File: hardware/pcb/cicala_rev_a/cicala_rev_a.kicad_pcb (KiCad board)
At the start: 4 copper layers, 78 x 45 mm, 0 parts

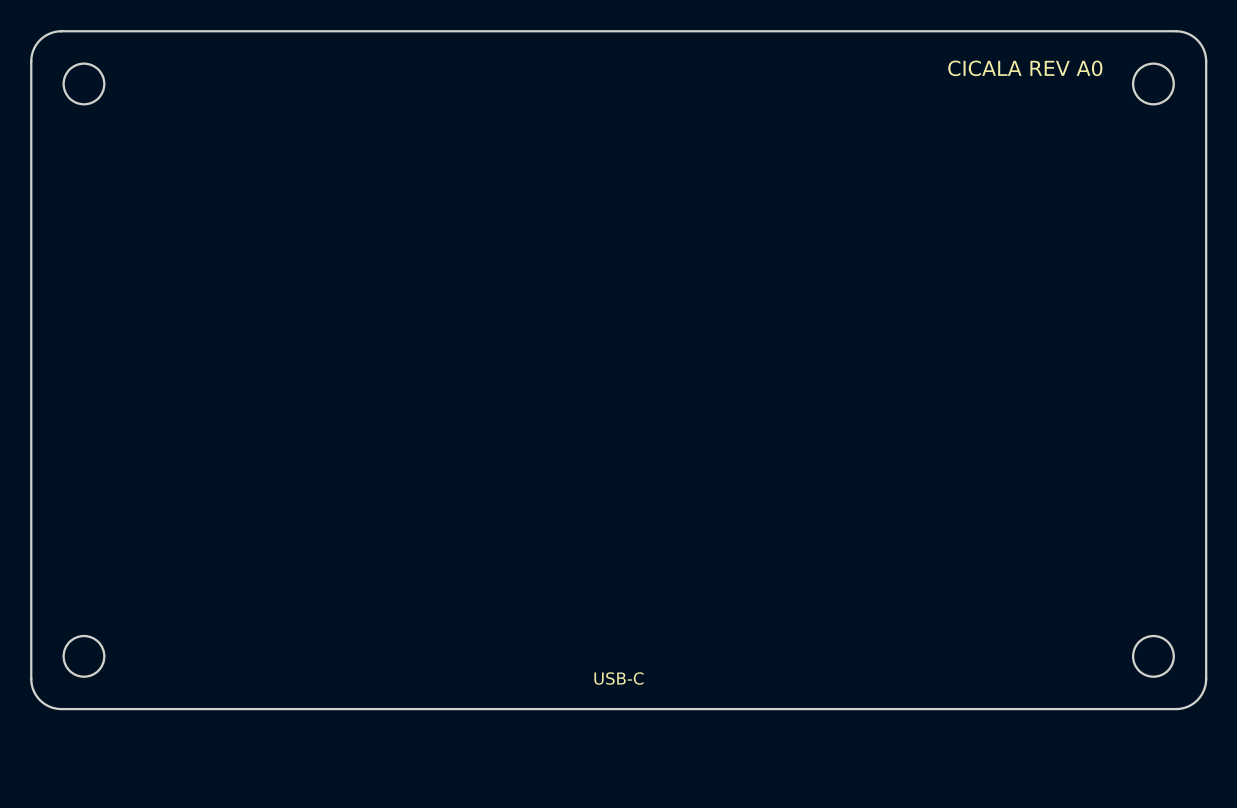
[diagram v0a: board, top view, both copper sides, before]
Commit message: feat(hw): place the Rev A board
Everything except the two switches and the display stack sits on the
underside, in the cell cavity, because the sloped roof leaves 0.8 to 3.5 mm
above the board. The module goes rear-left with its antenna at the board
edge and clear of the display; the cell keep-out, the power block and the
front connector row follow from that.

Placement is generated rather than dragged, so it can be regenerated after a
schematic change: anchors are chosen by hand, the rest are packed into free
regions ordered by distance to the pads they already share a net with.

Board is 78 x 49 mm at (3, 3.5). It grew 4 mm deeper than the old 78 x 45
because a USB-C plug could never have reached a receptacle sitting 6 mm
behind the case wall; the front edge now ends 1.5 mm from it and the
receptacle noses into the wall aperture.

Mounting holes become NPTH footprints instead of circles on Edge.Cuts, so
they are drilled rather than routed, and they move to x=13 to clear
Espressif's antenna keep-out, which the module footprint carries and which
reaches 9.5 mm in from the left edge.

J1 gets a project footprint whose silkscreen stops at the board edge; the
library outline would print past it, because the part deliberately overhangs.

Netclasses: Power 0.4 mm, USB 0.29 mm at a 0.29 mm gap for 90 ohm
differential over the declared 0.18 mm prepreg, HV 0.2 mm, which is the gap
the panel's own 0.5 mm-pitch connector allows.

DRC reports zero violations and zero schematic-parity issues. The 216
unconnected items are the routing, which is the next commit.

Co-Authored-By: Claude Opus 5 <noreply@anthropic.com>
Claude-Session: https://claude.ai/code/session_01E5vy1HJsPztSk9nFw6j5Ko
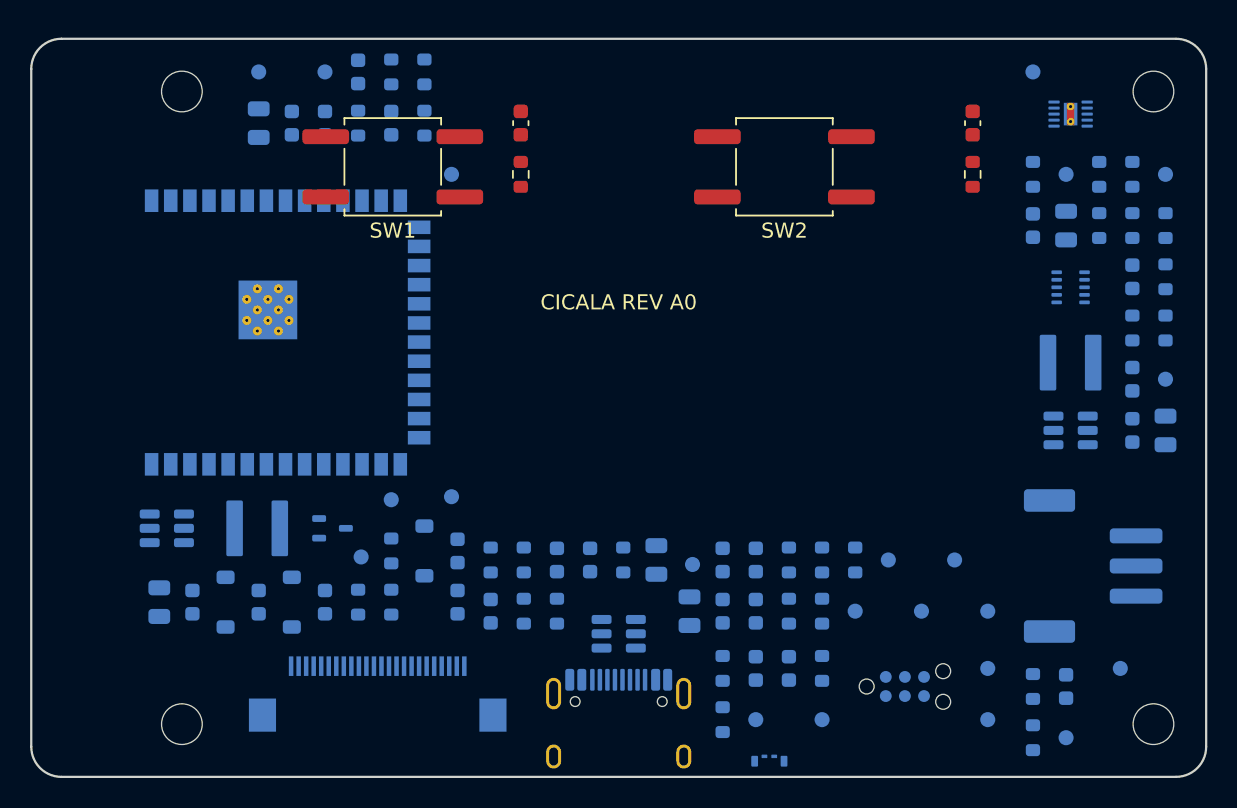
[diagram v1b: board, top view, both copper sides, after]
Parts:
- added C1: 3pF DNP, Capacitor_SMD:C_0603_1608Metric, B.Cu at (37.9, 38.1)
- added C10: 47uF 6.3V, Capacitor_SMD:C_0805_2012Metric, B.Cu at (78.3, 29.5)
- added C11: 100nF, Capacitor_SMD:C_0603_1608Metric, B.Cu at (76.1, 26.1)
- added C12: 1uF, Capacitor_SMD:C_0603_1608Metric, B.Cu at (22.5, 40.9)
- added C13: 10uF, Capacitor_SMD:C_0603_1608Metric, B.Cu at (18.1, 40.9)
- added C14: 1nF, Capacitor_SMD:C_0603_1608Metric, B.Cu at (13.7, 40.9)
- added C15: 4.7uF 25V, Capacitor_SMD:C_0805_2012Metric, B.Cu at (11.5, 40.9)
- added C16: 4.7uF 25V, Capacitor_SMD:C_0805_2012Metric, B.Cu at (44.5, 38.1)
- added C17: 1uF 25V, Capacitor_SMD:C_0603_1608Metric, B.Cu at (31.3, 40.9)
- added C18: 1uF 25V, Capacitor_SMD:C_0603_1608Metric, B.Cu at (33.5, 41.5)
- added C19: 1uF 25V, Capacitor_SMD:C_0603_1608Metric, B.Cu at (31.3, 37.5)
- added C2: 3pF DNP, Capacitor_SMD:C_0603_1608Metric, B.Cu at (40.1, 38.1)
- added C20: 1uF 25V, Capacitor_SMD:C_0603_1608Metric, B.Cu at (48.9, 41.5)
- added C21: 1uF 25V, Capacitor_SMD:C_0603_1608Metric, B.Cu at (51.1, 45.3)
- added C22: 1uF 25V, Capacitor_SMD:C_0603_1608Metric, B.Cu at (51.1, 41.5)
- added C23: 1uF 25V, Capacitor_SMD:C_0603_1608Metric, B.Cu at (51.1, 38.1)
- added C24: 1uF 25V, Capacitor_SMD:C_0603_1608Metric, B.Cu at (53.3, 45.3)
- added C25: 10nF, Capacitor_SMD:C_0603_1608Metric, F.Cu at (35.5, 9.10)
- added C26: 10nF, Capacitor_SMD:C_0603_1608Metric, F.Cu at (65.5, 9.10)
- added C27: 1uF, Capacitor_SMD:C_0603_1608Metric, B.Cu at (26.9, 9.10)
- added C28: 100nF, Capacitor_SMD:C_0603_1608Metric, B.Cu at (20.3, 9.10)
- added C29: 10uF, Capacitor_SMD:C_0603_1608Metric, B.Cu at (22.5, 9.10)
- added C3: 100nF, Capacitor_SMD:C_0603_1608Metric, B.Cu at (24.7, 5.70)
- added C30: 47uF, Capacitor_SMD:C_0805_2012Metric, B.Cu at (18.1, 9.10)
- added C31: 1nF 2kV, Capacitor_SMD:C_0805_2012Metric, B.Cu at (46.7, 41.5)
- added C4: 1uF 25V, Capacitor_SMD:C_0603_1608Metric, B.Cu at (48.9, 38.1)
- added C5: 10uF 25V, Capacitor_SMD:C_0805_2012Metric, B.Cu at (71.7, 15.9)
- added C6: 1uF 10V, Capacitor_SMD:C_0603_1608Metric, B.Cu at (69.5, 15.9)
- added C7: 100nF, Capacitor_SMD:C_0603_1608Metric, B.Cu at (71.7, 46.5)
- added C8: 10uF 6.3V, Capacitor_SMD:C_0603_1608Metric, B.Cu at (76.1, 19.3)
- added C9: 22uF 6.3V, Capacitor_SMD:C_0603_1608Metric, B.Cu at (76.1, 29.5)
- added D1: MBR0530, Diode_SMD:D_SOD-123, B.Cu at (20.3, 40.9)
- added D2: MBR0530, Diode_SMD:D_SOD-123, B.Cu at (15.9, 40.9)
- added D3: MBR0530, Diode_SMD:D_SOD-123, B.Cu at (29.1, 37.5)
- added D4: APBA2006SURKCGKC red/green, cicala:LED_Kingbright_APBA2006SURKCGKC, B.Cu at (52.0, 51.3)
- added H1: M2.5, MountingHole_2.7mm, F.Cu at (13.0, 7.00)
- added H2: M2.5, MountingHole_2.7mm, F.Cu at (77.5, 7.00)
- added H3: M2.5, MountingHole_2.7mm, F.Cu at (13.0, 49.0)
- added H4: M2.5, MountingHole_2.7mm, F.Cu at (77.5, 49.0)
- added J1: USB-C receptacle, cicala:USB_C_Receptacle_HRO_TYPE-C-31-M-12_EdgeOverhang, B.Cu at (42.0, 50.1)
- added J2: GDEY0213B74, Connector_FFC-FPC:Hirose_FH12-24S-0.5SH_1x24-1MP_P0.50mm_Horizontal, B.Cu at (26.0, 47.0)
- added J3: Protected LiPo + NTC, Connector_JST:JST_PH_S3B-PH-SM4-TB_1x03-1MP_P2.00mm_Horizontal, B.Cu at (73.5, 38.5)
- added J4: TC2030 recovery pads, Connector:Tag-Connect_TC2030-IDC-NL_2x03_P1.27mm_Vertical, B.Cu at (61.0, 46.5)
- added L1: 47uH VLS4012CX-470M-1, cicala:L_TDK_VLS4012, B.Cu at (18.0, 36.0)
- added L2: 0.47uH XFL4015-471ME, cicala:L_Coilcraft_XFL4015, B.Cu at (72.0, 25.0)
- added Q1: Si1308EDL, Package_TO_SOT_SMD:SOT-323_SC-70, B.Cu at (23.0, 36.0)
- added R1: 5.1k, Resistor_SMD:R_0603_1608Metric, B.Cu at (48.9, 45.3)
- added R10: 10k, Resistor_SMD:R_0603_1608Metric, B.Cu at (73.9, 15.9)
- added R11: 1M, Resistor_SMD:R_0603_1608Metric, B.Cu at (69.5, 46.5)
- added R12: 470k, Resistor_SMD:R_0603_1608Metric, B.Cu at (69.5, 49.9)
- added R13: 100k, Resistor_SMD:R_0603_1608Metric, B.Cu at (76.1, 15.9)
- added R14: 511k 1%, Resistor_SMD:R_0603_1608Metric, B.Cu at (76.1, 22.7)
- added R15: 91k 1%, Resistor_SMD:R_0603_1608Metric, B.Cu at (78.3, 19.3)
- added R16: 100k, Resistor_SMD:R_0603_1608Metric, B.Cu at (78.3, 15.9)
- added R18: 150, Resistor_SMD:R_0603_1608Metric, B.Cu at (26.9, 37.5)
- added R19: 1M, Resistor_SMD:R_0603_1608Metric, B.Cu at (26.9, 40.9)
- added R2: 5.1k, Resistor_SMD:R_0603_1608Metric, B.Cu at (37.9, 41.5)
- added R20: 2.2, Resistor_SMD:R_0603_1608Metric, B.Cu at (24.7, 40.9)
- added R21: 47k, Resistor_SMD:R_0603_1608Metric, F.Cu at (35.5, 12.5)
- added R22: 47k, Resistor_SMD:R_0603_1608Metric, F.Cu at (65.5, 12.5)
- added R23: 1k, Resistor_SMD:R_0603_1608Metric, B.Cu at (42.3, 38.1)
- added R24: 1k, Resistor_SMD:R_0603_1608Metric, B.Cu at (35.7, 41.5)
- added R25: 10k, Resistor_SMD:R_0603_1608Metric, B.Cu at (29.1, 9.10)
- added R26: 10k, Resistor_SMD:R_0603_1608Metric, B.Cu at (24.7, 9.10)
- added R27: 470, Resistor_SMD:R_0603_1608Metric, B.Cu at (53.3, 38.1)
- added R28: 470, Resistor_SMD:R_0603_1608Metric, B.Cu at (53.3, 41.5)
- added R29: 470, Resistor_SMD:R_0603_1608Metric, B.Cu at (55.5, 38.1)
- added R3: 22, Resistor_SMD:R_0603_1608Metric, B.Cu at (35.7, 38.1)
- added R30: 470, Resistor_SMD:R_0603_1608Metric, B.Cu at (55.5, 41.5)
- added R31: 470, Resistor_SMD:R_0603_1608Metric, B.Cu at (57.7, 38.1)
- added R32: 1M, Resistor_SMD:R_0603_1608Metric, B.Cu at (55.5, 45.3)
- added R33: 0, Resistor_SMD:R_0603_1608Metric, B.Cu at (48.9, 48.7)
- added R34: 0, Resistor_SMD:R_0603_1608Metric, B.Cu at (78.3, 22.7)
- added R4: 22, Resistor_SMD:R_0603_1608Metric, B.Cu at (33.5, 38.1)
- added R5: 100k, Resistor_SMD:R_0603_1608Metric, B.Cu at (29.1, 5.70)
- added R6: 150k, Resistor_SMD:R_0603_1608Metric, B.Cu at (26.9, 5.70)
- added R7: 18k, Resistor_SMD:R_0603_1608Metric, B.Cu at (73.9, 12.5)
- added R8: 1.20k, Resistor_SMD:R_0603_1608Metric, B.Cu at (76.1, 12.5)
- added R9: 10k, Resistor_SMD:R_0603_1608Metric, B.Cu at (69.5, 12.5)
- added SW1: CATEGORY KSC321GLFS, Button_Switch_SMD:SW_Push_1P1T_NO_CK_KSC6xxG, F.Cu at (27.0, 12.0)
- added SW2: NEXT KSC321GLFS, Button_Switch_SMD:SW_Push_1P1T_NO_CK_KSC6xxG, F.Cu at (53.0, 12.0)
- added TP1: BOOT_IO0, TestPoint:TestPoint_Pad_D1.0mm, B.Cu at (18.1, 5.70)
- added TP10: USB_VBUS, TestPoint:TestPoint_Pad_D1.0mm, B.Cu at (59.9, 38.1)
- added TP11: REG_PG, TestPoint:TestPoint_Pad_D1.0mm, B.Cu at (75.3, 45.3)
- added TP12: USB_DP, TestPoint:TestPoint_Pad_D1.0mm, B.Cu at (51.1, 48.7)
- added TP13: USB_DN, TestPoint:TestPoint_Pad_D1.0mm, B.Cu at (57.7, 41.5)
- added TP14: CHG_STAT1, TestPoint:TestPoint_Pad_D1.0mm, B.Cu at (69.5, 5.70)
- added TP15: CHG_STAT2, TestPoint:TestPoint_Pad_D1.0mm, B.Cu at (66.5, 45.3)
- added TP16: PNL_CLK, TestPoint:TestPoint_Pad_D1.0mm, B.Cu at (26.9, 34.1)
- added TP17: PNL_MOSI, TestPoint:TestPoint_Pad_D1.0mm, B.Cu at (55.5, 48.7)
- added TP18: PNL_CS, TestPoint:TestPoint_Pad_D1.0mm, B.Cu at (62.1, 41.5)
- added TP19: PNL_DC, TestPoint:TestPoint_Pad_D1.0mm, B.Cu at (64.3, 38.1)
- added TP2: CHIP_EN, TestPoint:TestPoint_Pad_D1.0mm, B.Cu at (30.9, 12.5)
- added TP20: PNL_RESET, TestPoint:TestPoint_Pad_D1.0mm, B.Cu at (66.5, 41.5)
- added TP21: EPD_BUSY, TestPoint:TestPoint_Pad_D1.0mm, B.Cu at (22.5, 5.70)
- added TP22: VBAT_CELL, TestPoint:TestPoint_Pad_D1.0mm, B.Cu at (78.3, 26.1)
- added TP3: GND, TestPoint:TestPoint_Pad_D1.0mm, B.Cu at (66.5, 48.7)
- added TP4: UART0_TX, TestPoint:TestPoint_Pad_D1.0mm, B.Cu at (46.9, 38.4)
- added TP5: UART0_RX, TestPoint:TestPoint_Pad_D1.0mm, B.Cu at (30.9, 33.9)
- added TP6: FACTORY_RESET_OD, TestPoint:TestPoint_Pad_D1.0mm, B.Cu at (24.9, 37.9)
- added TP7: 3V3, TestPoint:TestPoint_Pad_D1.0mm, B.Cu at (71.7, 49.9)
- added TP8: VBAT, TestPoint:TestPoint_Pad_D1.0mm, B.Cu at (71.7, 12.5)
- added TP9: VSYS, TestPoint:TestPoint_Pad_D1.0mm, B.Cu at (78.3, 12.5)
- added U1: ESP32-S3-WROOM-1-N16 / WROOM-1U-N16, RF_Module:ESP32-S3-WROOM-1, B.Cu at (16.2, 23.0)
- added U2: BQ25185DLH, Package_DFN_QFN:Texas_DLH0010A_WSON-10-1EP_2.2x2mm_P0.4mm_EP0.9x1.5mm_ThermalVias, B.Cu at (72.0, 8.50)
- added U3: TPS63802DLA, cicala:Texas_DLA0010A_VSON-HR-10_2x3mm_P0.5mm, B.Cu at (72.0, 20.0)
- added U4: USBLC6-2SC6, Package_TO_SOT_SMD:SOT-23-6, B.Cu at (42.0, 43.0)
- added U5: TPS22917DBVR, Package_TO_SOT_SMD:SOT-23-6, B.Cu at (72.0, 29.5)
- added U6: TPS22917DBVR, Package_TO_SOT_SMD:SOT-23-6, B.Cu at (12.0, 36.0)
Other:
- board size 78 x 45 mm -> 78 x 49 mm
- board text added: "ANTENNA - NO COPPER / METAL"
- board text added: "MODULE UNDERSIDE"
- board text removed: "ANTENNA — NO COPPER / METAL"
- board text removed: "CONSTRAINT SKELETON — NOT FOR FABRICATION"
- board text removed: "FPC DATUM — VERIFY FOOTPRINT"
- board text removed: "USB-C"
- board text removed: "WROOM-1 CONFLICT / 1U BASELINE"

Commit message: feat(hw): route the Rev A board, and correct three part ratings
Board work. The layer plan is F.Cu and B.Cu for signals with a ground pour,
In1.Cu as an unbroken ground reference, and In2.Cu carrying the 3V3 plane,
signals, and a ground island under the USB pair so that pair is referenced to
ground rather than to the rail. Two signal layers were not enough for 105
parts on 78 x 49 mm.

Placement and routing are generated by hardware/pcb/tools/ rather than dragged
by hand, so they can be regenerated after a schematic change and read as a
diff. The router is a grid maze router with hard blocking, so clearance is a
property of the search rather than something checked afterwards. Getting that
right took finding five modelling errors, each recorded in tools/README.md;
the one that mattered most is that copper modelled as grid cells can extend
half a cell past the outermost cell centre, so every clearance radius has to
carry that slack. Ignoring it produced violations the model could not see.

The board is not finished: 36 connections are unrouted and about 50 DRC
violations remain, mostly pour artifacts around the unrouted areas. The
READMEs say so rather than implying otherwise.

Part ratings, each against the datasheet rather than by habit:

- C8 becomes 10 uF 25 V in 0805. SLUSF65B section 7.2.2.3 asks for 25 V parts
  on the charger's IN and SYS pins, and the TPS63802 wants 4 uF effective on
  VIN, which a 6.3 V part at 4.5 V does not reliably give.
- C6 becomes 1 uF 16 V, to keep useful capacitance at 4.2 V on the BAT pin.
- R7 at 18 kOhm and R8 at 1.20 kOhm are confirmed correct: table 6-1 gives
  4.2 V and a 500 mA input limit for 18 kOhm, and 300/1200 is 250 mA.
- The bi-colour LED is confirmed safe on 3.3 V through 1 kOhm: both dies are
  AlGaInP at 2.5 V maximum, so the green is not a 3.2 V InGaN part. Whether
  0.8 to 1.3 mA is bright enough through the light pipe is a bench question.

Also adds export_fab.sh for the Gerber, drill, pick-and-place, BOM, assembl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
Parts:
- C6: value 1uF 10V -> 1uF 16V
- C8: value 10uF 6.3V -> 10uF 25V; footprint Capacitor_SMD:C_0603_1608Metric -> Capacitor_SMD:C_0805_2012Metric
- moved TP17 57.0 mm to (18.1, 5.70)
- moved TP20 48.2 mm to (18.4, 38.9)
- moved TP3 47.5 mm to (20.3, 37.5)
- moved C14 39.6 mm to (53.3, 41.5)
- moved R12 37.0 mm to (33.5, 41.5)
- moved C7 36.3 mm to (35.7, 41.5)
- moved C15 35.3 mm to (46.7, 38.1)
- moved TP21 33.4 mm to (15.9, 38.4)
- moved TP5 33.2 mm to (59.9, 50.1)
- moved TP19 33.1 mm to (31.4, 41.9)
- moved C13 33.1 mm to (51.1, 38.1)
- moved R32 31.9 mm to (23.8, 42.0)
- moved R15 31.8 mm to (69.5, 49.9)
- moved R31 30.7 mm to (27.2, 42.0)
- moved TP16 28.7 mm to (22.5, 5.70)
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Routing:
- net USB_VBUS: track 0.00 -> 102.5 mm, vias 0 -> 10
- net CHG_STAT2: track 0.00 -> 84.1 mm, vias 0 -> 4
- net CHG_STAT1: track 0.00 -> 76.1 mm, vias 0 -> 4
- net BOOT_IO0: track 0.00 -> 66.4 mm, vias 0 -> 4
- net CHIP_EN: track 0.00 -> 66.1 mm, vias 0 -> 4
- net EPD_3V3: track 0.00 -> 62.4 mm, vias 0 -> 6
- net UART0_TX: track 0.00 -> 58.8 mm, vias 0 -> 5
- net VBAT_SENSE_EN: track 0.00 -> 57.1 mm, vias 0 -> 3
- net PNL_MOSI: track 0.00 -> 56.7 mm, vias 0 -> 2
- net UART0_RX: track 0.00 -> 53.5 mm, vias 0 -> 2
- net PNL_CLK: track 0.00 -> 50.1 mm, vias 0 -> 2
- net EPD_DC: track 0.00 -> 49.0 mm, vias 0 -> 3
- net Net-(U3-FB): track 0.00 -> 48.0 mm
- net CHG_ENABLE: track 0.00 -> 47.7 mm, vias 0 -> 2
- net VBAT_SENSE: track 0.00 -> 47.0 mm, vias 0 -> 5
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- added copper zone on In2.Cu, net 3V3
- added copper zone on B.Cu, net GND
- added copper zone on F.Cu, net GND
- added copper zone on In1.Cu, net GND
- added copper zone on In2.Cu, net GND
